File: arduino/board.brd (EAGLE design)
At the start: 50.8 x 71.1 mm, 13 parts

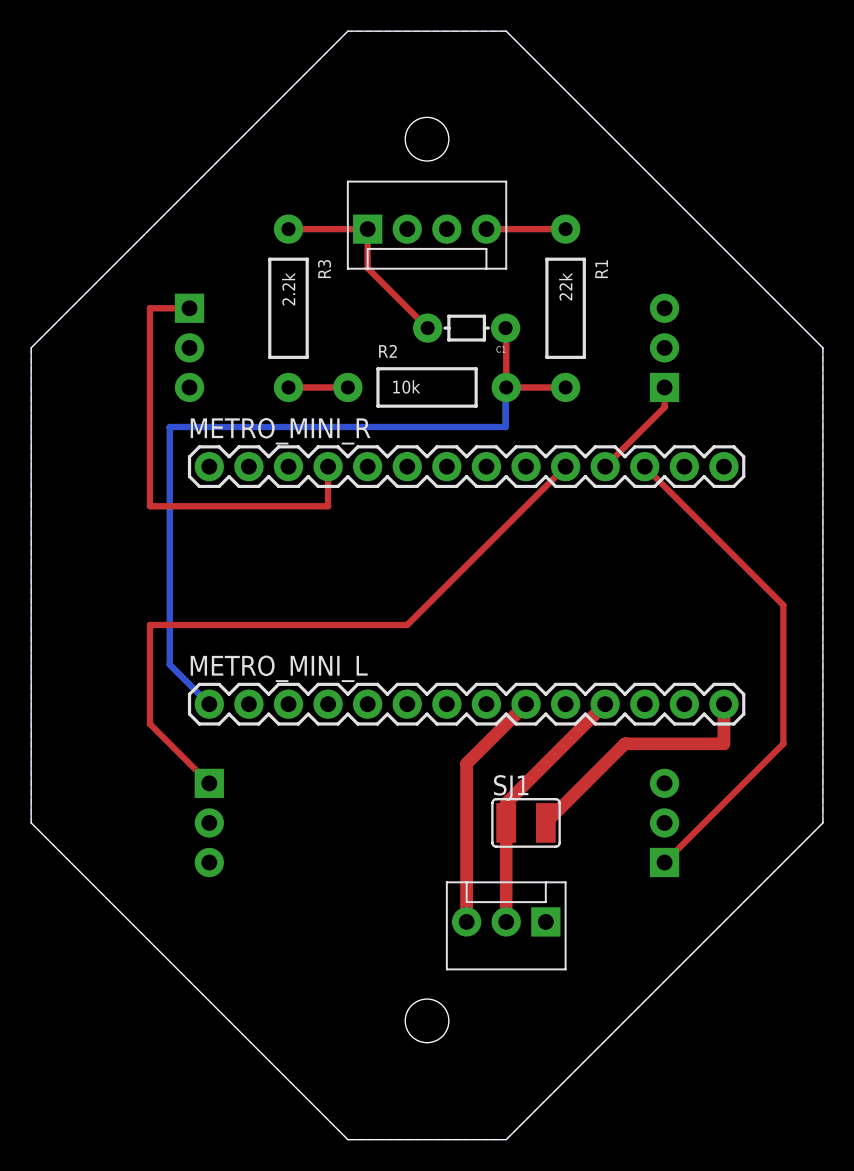
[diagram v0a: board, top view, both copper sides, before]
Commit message: Flip board and make ready to build
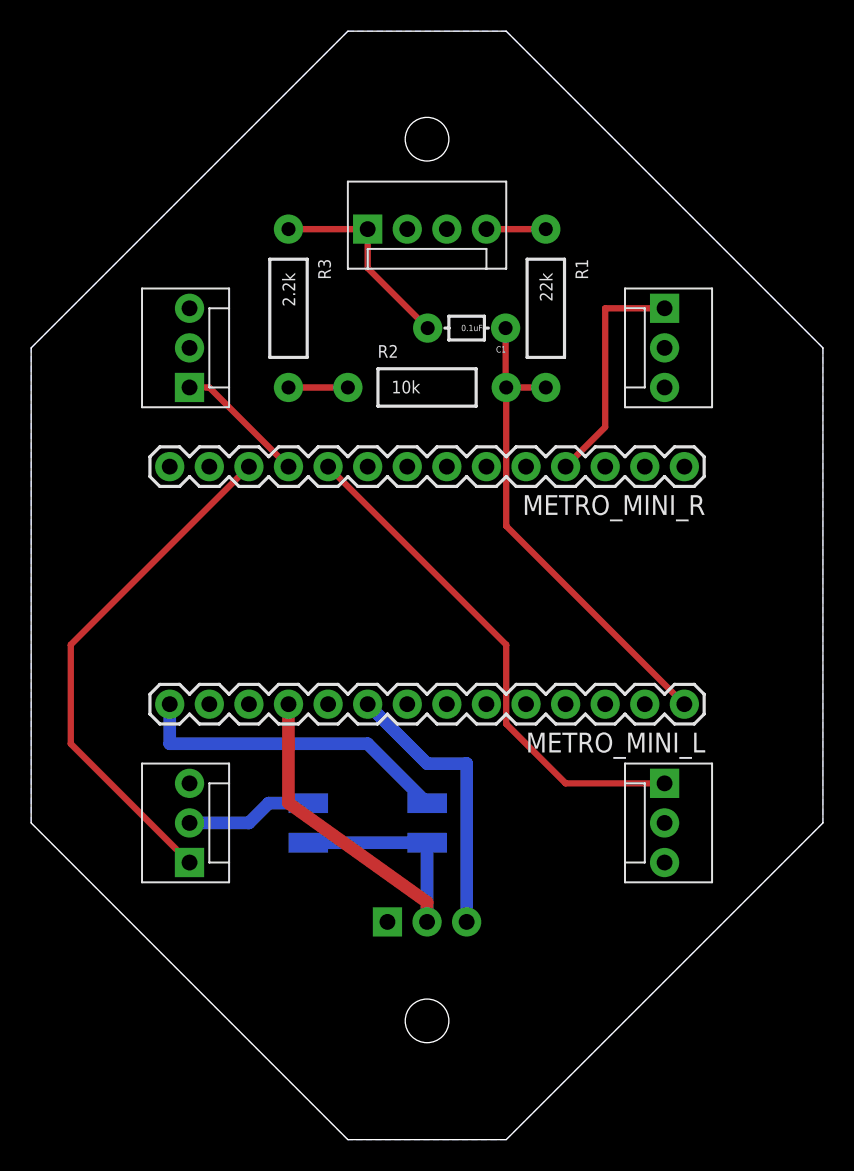
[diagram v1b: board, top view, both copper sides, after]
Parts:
- removed SJ1: (no value), jumper:SJW
- added PWR3, USB: (no value), jumper:SJW
- C1: value (none) -> 0.1uF
- moved ESC1 30.5 mm to (40.6, 53.3), flipped to the top
- moved ESC2 30.5 mm to (10.2, 48.3), flipped to the top
- moved ESC3 30.5 mm to (10.2, 17.8), flipped to the top
- moved METRO_MINI_L 30.5 mm to (41.9, 27.9), turned to 180 degrees
- moved METRO_MINI_R 30.5 mm to (41.9, 43.2), turned to 180 degrees
- moved ESC4 29.2 mm to (40.6, 22.9), flipped to the top
- moved PWR 10.2 mm to (22.9, 14.0), flipped to the bottom
- moved R1 1.27 mm to (33.0, 53.3)
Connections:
- new net N$2: ESC3.2, PWR3.2
- net 5V: now also PWR3.1, USB.1; no longer SJ1.1
- net USB: now also USB.2; no longer SJ1.2
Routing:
- net A5: track 50.6 -> 31.4 mm
- net 5V: track 16.6 -> 31.2 mm
- net D3: track 29.2 -> 15.0 mm
- net D9: track 42.6 -> 33.0 mm
- net N$2: track 0.00 -> 8.15 mm
- net USB: track 16.1 -> 20.6 mm
- net GND: track 28.6 -> 31.1 mm
- net D10: track 6.66 -> 8.45 mm
- net VBAT: track 5.08 -> 3.81 mm
- net D11: track 32.2 -> 33.3 mm
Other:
- board text added: "ESC1"
- board text added: "ESC2"
- board text added: "ESC3"
- board text added: "ESC4"
- board text removed: "Note: All the parts should be mounted on the bottom side"
